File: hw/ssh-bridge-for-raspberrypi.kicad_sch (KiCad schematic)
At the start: 38 parts, among them J101 USB4105-GF-A, J102 USB4105-GF-A, J103 PinHeader Conn_01x08, J104 Conn_02x05_Odd_Even, J105 USB_A, J106 Conn_01x03, SW304 1, U101 ST7789V_TFT_DISPLAY, U102 TLP3555A, U103 AZ1117-CH3.3TRG1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

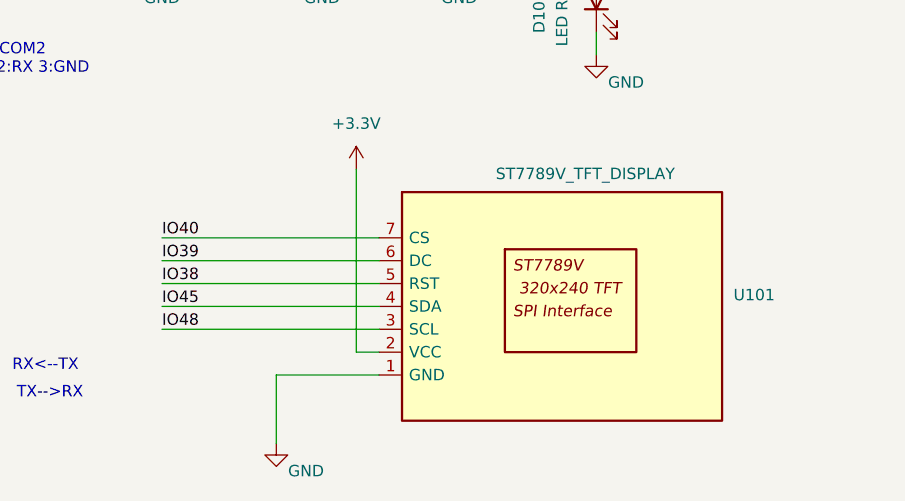
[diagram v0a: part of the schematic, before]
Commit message: Update ST7789V new 8pin foot print
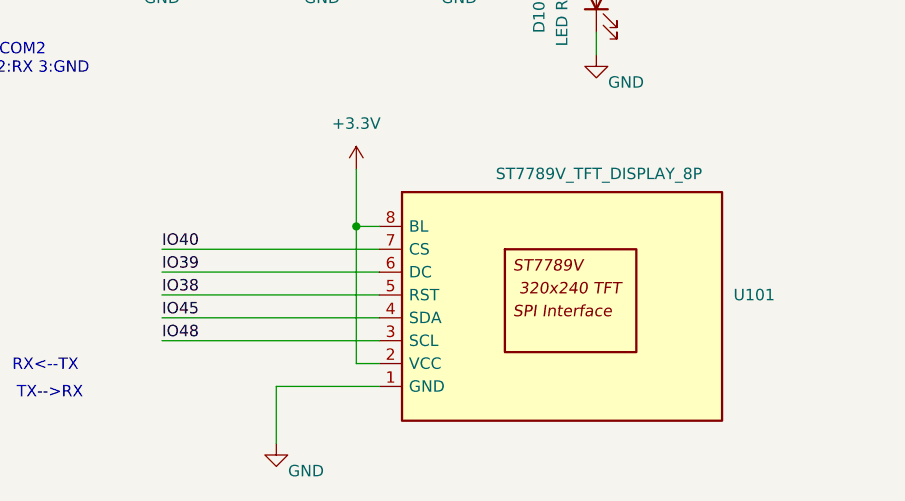
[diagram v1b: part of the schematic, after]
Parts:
- J105: footprint Library:USB_C_5077CR-16-SMC2-BK-TR -> Library:USB_A_5075AR-04
- U101: value ST7789V_TFT_DISPLAY -> ST7789V_TFT_DISPLAY_8P; footprint Library:ST7789V TFT SPI DISPLAY 320x240 -> Library:ST7789V TFT SPI DISPLAY 320x240 GMT020-02-8P
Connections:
- net +3.3V: now also U101.8 (BL)
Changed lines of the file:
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@@
 		(title "SSH SERIAL BRDGE AND VIEWER")
 		(date "2026-04-05")
-		(rev "Rev2")
+		(rev "Rev3")
 		(company "HNZ")
 		(comment 1 "Licensed under CC-BY-SA V4.0")
@@
 	)
 	(junction
+		(at 97.79 161.29)
+		(diameter 0)
+		(color 0 0 0 0)
+	)
+	(junction
 		(at 210.82 88.9)
 		(diameter 0)
@@
 	(wire
 		(pts
-			(xy 76.2 165.1) (xy 100.33 165.1)
+			(xy 76.2 166.37) (xy 100.33 166.37)
 		)
 		(stroke
@@
 	(wire
 		(pts
-			(xy 100.33 175.26) (xy 97.79 175.26)
+			(xy 100.33 176.53) (xy 97.79 176.53)
 		)
 		(stroke
@@
 	(wire
 		(pts
-			(xy 76.2 172.72) (xy 100.33 172.72)
+			(xy 76.2 173.99) (xy 100.33 173.99)
 		)
 		(stroke
@@
 	(wire
 		(pts
-			(xy 100.33 177.8) (xy 88.9 177.8)
+			(xy 100.33 179.07) (xy 88.9 179.07)
 		)
 		(stroke
@@
 	(wire
 		(pts
-			(xy 76.2 167.64) (xy 100.33 167.64)
+			(xy 76.2 168.91) (xy 100.33 168.91)
 		)
 		(stroke
@@
 	(wire
 		(pts
+			(xy 97.79 161.29) (xy 100.33 161.29)
+		)
+		(stroke
+			(width 0)
+			(type default)
+		)
+	)
+	(wire
+		(pts
 			(xy 158.75 114.3) (xy 158.75 119.38)
 		)
@@
 	(wire
 		(pts
+			(xy 97.79 161.29) (xy 97.79 176.53)
+		)
+		(stroke
+			(width 0)
+			(type default)
+		)
+	)
+	(wire
+		(pts
 			(xy 68.58 50.8) (xy 91.44 50.8)
 		)
@@
 	(wire
 		(pts
-			(xy 88.9 177.8) (xy 88.9 185.42)
+			(xy 88.9 179.07) (xy 88.9 185.42)
 		)
 		(stroke
@@
 	(wire
 		(pts
-			(xy 76.2 162.56) (xy 100.33 162.56)
+			(xy 76.2 163.83) (xy 100.33 163.83)
 		)
 		(stroke
@@
 	(wire
 		(pts
-			(xy 97.79 154.94) (xy 97.79 175.26)
+			(xy 97.79 154.94) (xy 97.79 161.29)
 		)
 		(stroke
@@
 	(wire
 		(pts
-			(xy 76.2 170.18) (xy 100.33 170.18)
+			(xy 76.2 171.45) (xy 100.33 171.45)
 		)
 		(stroke
@@
 	)
 	(label "IO39"
-		(at 76.2 165.1 0)
+		(at 76.2 166.37 0)
 		(effects
 			(font
@@
 	)
 	(label "IO48"
-		(at 76.2 172.72 0)
+		(at 76.2 173.99 0)
 		(effects
 			(font
@@
 	)
 	(label "IO45"
-		(at 76.2 170.18 0)
+		(at 76.2 171.45 0)
 		(effects
 			(font
@@
 	)
 	(label "IO38"
-		(at 76.2 167.64 0)
+		(at 76.2 168.91 0)
 		(effects
 			(font
@@
 	)
 	(label "IO40"
-		(at 76.2 162.56 0)
+		(at 76.2 163.83 0)
 		(effects
 			(font
@@
 			)
 		)
-		(property "Footprint" "Library:USB_C_5077CR-16-SMC2-BK-TR"
+		(property "Footprint" "Library:USB_A_5075AR-04"
 			(at 256.54 92.71 0)
 			(hide yes)
@@
 			)
 		)
-		(property "Value" "ST7789V_TFT_DISPLAY"
+		(property "Value" "ST7789V_TFT_DISPLAY_8P"
 			(at 113.284 155.448 0)
 			(show_name no)
@@
 			)
 		)
-		(property "Footprint" "Library:ST7789V TFT SPI DISPLAY 320x240"
+		(property "Footprint" "Library:ST7789V TFT SPI DISPLAY 320x240 GMT020-02-8P"
 			(at 120.65 187.96 0)
 			(hide yes)
@@
 		(pin "2"
 		)
+		(pin "8"
+		)
 		(instances
